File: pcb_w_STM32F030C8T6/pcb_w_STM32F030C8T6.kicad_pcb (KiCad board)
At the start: 2 copper layers, 32 parts, among them J1 Conn_01x04, J2 Conn_01x05, J3 USB_B_Micro, SW1 SW_Push, SW2 SW_SPDT, SW3 SW_Push, SW4 SW_Push, SW5 SW_Push, U1 STM32F030C8Tx, U2 IFX27001TFV33

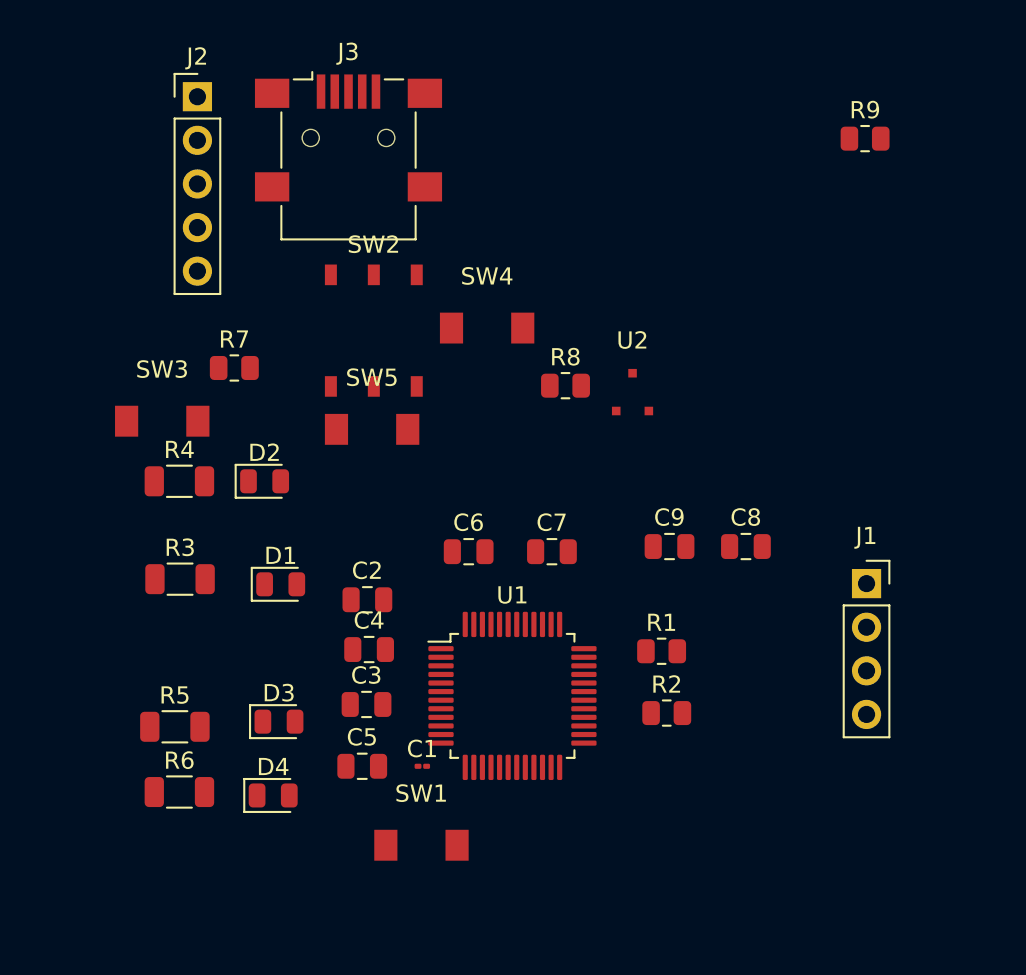
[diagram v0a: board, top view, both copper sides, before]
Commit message: made board 4 layers
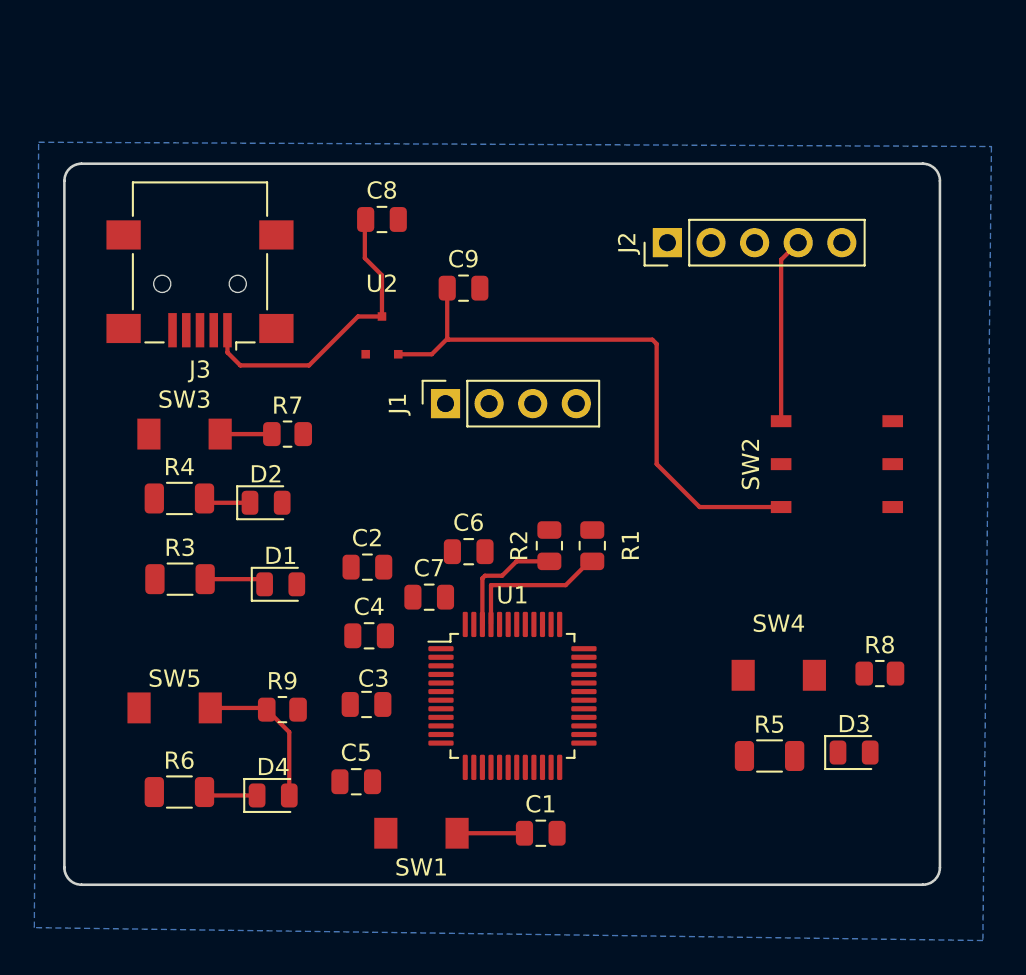
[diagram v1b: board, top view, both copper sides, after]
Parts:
- C1: footprint Capacitor_SMD:C_01005_0402Metric -> Capacitor_SMD:C_0805_2012Metric
- moved R9 47.5 mm to (55.7, 97.8)
- moved R5 34.7 mm to (84.1, 100.5)
- moved D3 33.5 mm to (89.0, 100.3)
- moved J2 28.7 mm to (78.1, 70.6), turned to 90 degrees
- moved C8 28.5 mm to (61.5, 69.2)
- moved SW2 28.1 mm to (88.0, 83.5), turned to 90 degrees
- moved J1 26.7 mm to (65.2, 80.0), turned to 90 degrees
- moved SW4 26.4 mm to (84.6, 95.8)
- moved R8 24.8 mm to (90.5, 95.7)
- moved SW5 19.9 mm to (49.4, 97.7)
- moved C9 19.2 mm to (66.2, 73.2)
- moved U2 15.0 mm to (61.5, 76.0)
- moved J3 12.1 mm to (50.9, 73.0), turned to 180 degrees
- moved R2 11.9 mm to (71.2, 88.2), turned to 90 degrees
- moved C1 7.93 mm to (70.8, 105.0)
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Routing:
- net MC_USB_3.3: track 0.00 -> 33.8 mm
- net MC_USB_5: track 0.00 -> 17.9 mm
- net Net-(J2-Pad4): track 0.00 -> 10.8 mm
- net DEC: track 0.00 -> 8.87 mm
- net SCL: track 0.00 -> 8.76 mm
- net SDA: track 0.00 -> 7.00 mm
- net NRST: track 0.00 -> 3.92 mm
- net Net-(D1-Pad1): track 0.00 -> 3.59 mm
- net Net-(D4-Pad1): track 0.00 -> 3.15 mm
- net CHANGE_STATE: track 0.00 -> 3.01 mm
- net Net-(D2-Pad1): track 0.00 -> 2.75 mm
- added copper zone on B.Cu, net GND
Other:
- board outline added: 51 x 42 mm

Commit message: saved
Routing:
- added copper zone on In1.Cu, net VDDA
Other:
- copper layers 2 -> 4
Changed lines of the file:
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@@
 (kicad_pcb (version 20211014) (generator pcbnew)
   (general
-    (thickness 1.6)
+    (thickness 4.69)
   )
   (paper "A4")
   (layers
     (0 "F.Cu" signal)
+    (1 "In1.Cu" signal)
+    (2 "In2.Cu" signal)
     (31 "B.Cu" signal)
     (32 "B.Adhes" user "B.Adhesive")
@@
       (layer "F.Cu" (type "copper") (thickness 0.035))
       (layer "dielectric 1" (type "core") (thickness 1.51) (material "FR4") (epsilon_r 4.5) (loss_tangent 0.02))
+      (layer "In1.Cu" (type "copper") (thickness 0.035))
+      (layer "dielectric 2" (type "prepreg") (thickness 1.51) (material "FR4") (epsilon_r 4.5) (loss_tangent 0.02))
+      (layer "In2.Cu" (type "copper") (thickness 0.035))
+      (layer "dielectric 3" (type "core") (thickness 1.51) (material "FR4") (epsilon_r 4.5) (loss_tangent 0.02))
       (layer "B.Cu" (type "copper") (thickness 0.035))
       (layer "B.Mask" (type "Bottom Solder Mask") (thickness 0.01))
@@
   (segment (start 77.25 76.25) (end 65.35 76.25) (width 0.25) (layer "F.Cu") (net 20))
   (segment (start 80 86) (end 77.5 83.5) (width 0.25) (layer "F.Cu") (net 20))
+  (zone (net 3) (net_name "VDDA") (layer "In1.Cu") (hatch edge 0.508)
+    (connect_pads (clearance 0.508))
+    (min_thickness 0.254) (filled_areas_thickness no)
+    (fill yes (thermal_gap 0.508) (thermal_bridge_width 0.508))
+    (polygon
+      (pts
+        (xy 97.043209 65.00317)
+        (xy 96.543209 111.25317)
+        (xy 41.293209 110.50317)
+        (xy 41.543209 64.75317)
+      )
+    )
+  )
   (zone (net 2) (net_name "GND") (layer "B.Cu") (hatch edge 0.508)
     (connect_pads (clearance 0.508))

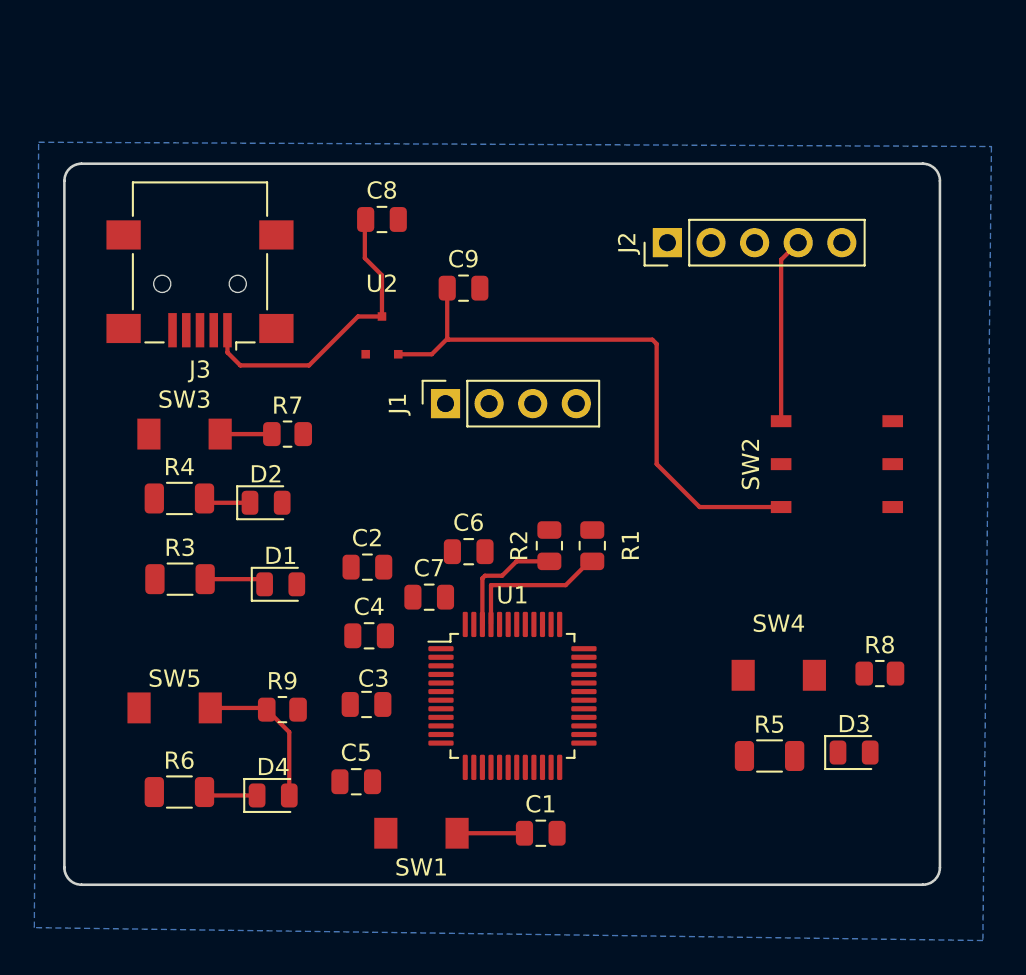
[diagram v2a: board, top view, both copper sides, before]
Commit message: finished routing...need to fix margins errors
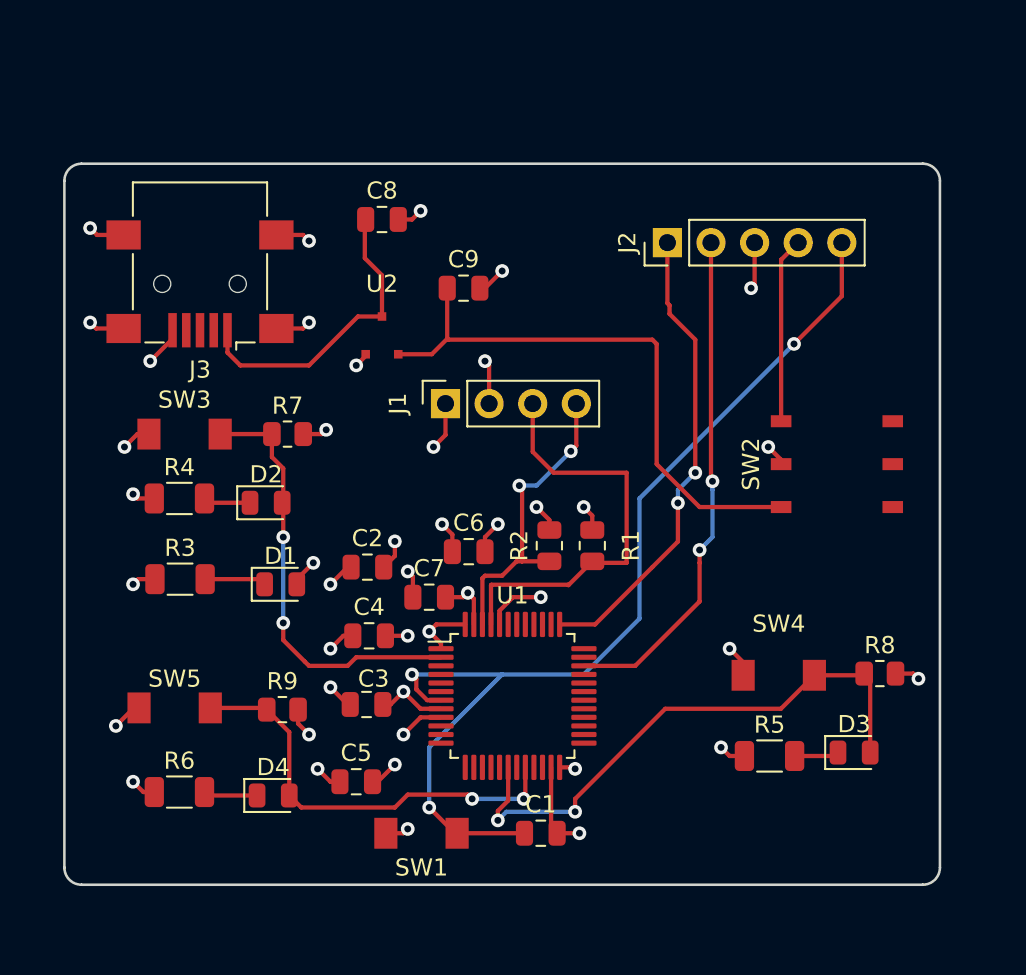
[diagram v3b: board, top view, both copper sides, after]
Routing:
- net NRST: track 3.92 -> 59.7 mm, vias 0 -> 3
- net GND: track 0.00 -> 55.1 mm, vias 0 -> 26
- net INC: track 0.00 -> 33.4 mm, vias 0 -> 2
- net VDDA: track 0.00 -> 31.1 mm, vias 0 -> 17
- net SWDIO: track 0.00 -> 29.5 mm, vias 0 -> 2
- net SWCLK: track 0.00 -> 27.4 mm, vias 0 -> 2
- net CHANGE_STATE: track 3.01 -> 25.4 mm, vias 0 -> 2
- net DEC: track 8.87 -> 25.1 mm, vias 0 -> 2
- net SCL: track 8.76 -> 24.8 mm
- net SDA: track 7.00 -> 18.2 mm, vias 0 -> 2
- net Net-(D3-Pad1): track 0.00 -> 2.61 mm
- added copper zone on In2.Cu, net GND
- removed copper zone on B.Cu, net GND

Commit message: finished routing and add silkscreen
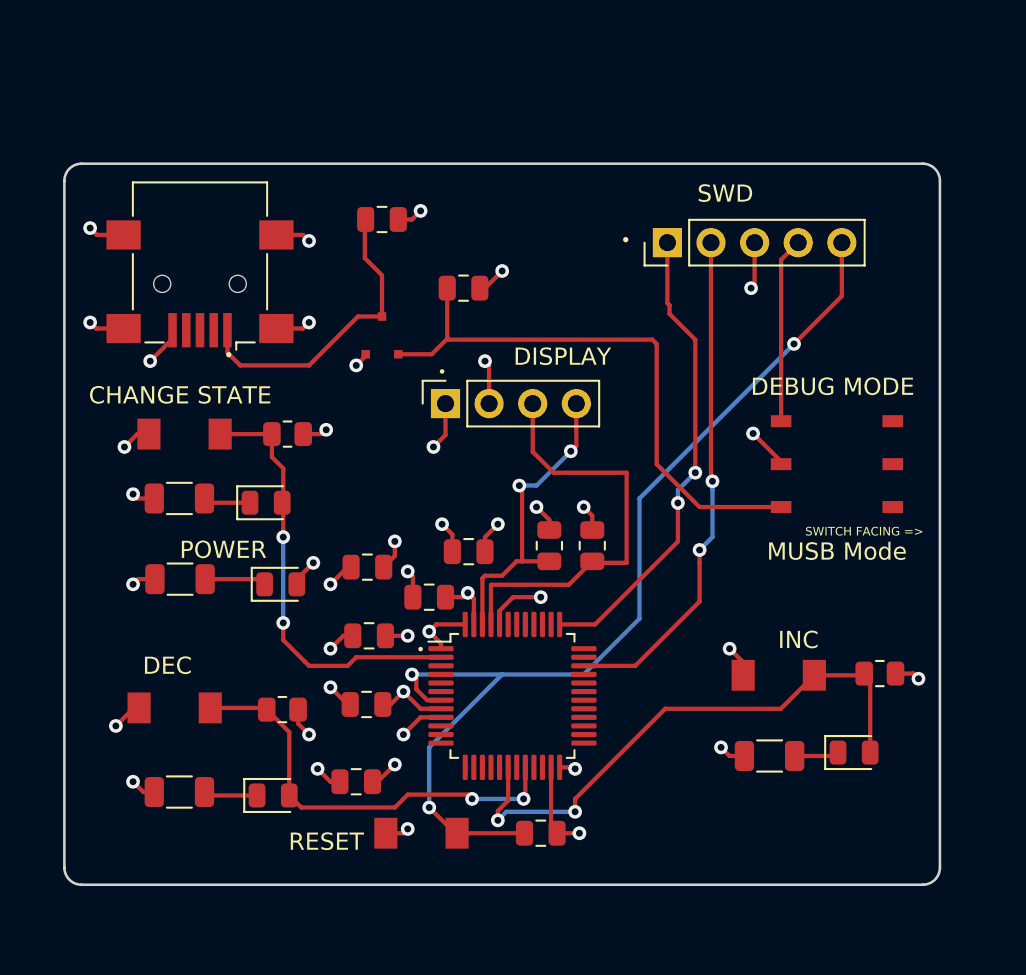
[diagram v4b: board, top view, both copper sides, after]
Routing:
- net VDDA: track 31.1 -> 32.2 mm
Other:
- board text added: "CHANGE STATE"
- board text added: "DEBUG MODE"
- board text added: "DEC"
- board text added: "DISPLAY"
- board text added: "INC"
- board text added: "MUSB Mode"
- board text added: "POWER"
- board text added: "RESET"
- board text added: "SWD"
- board text added: "SWITCH FACING =>"

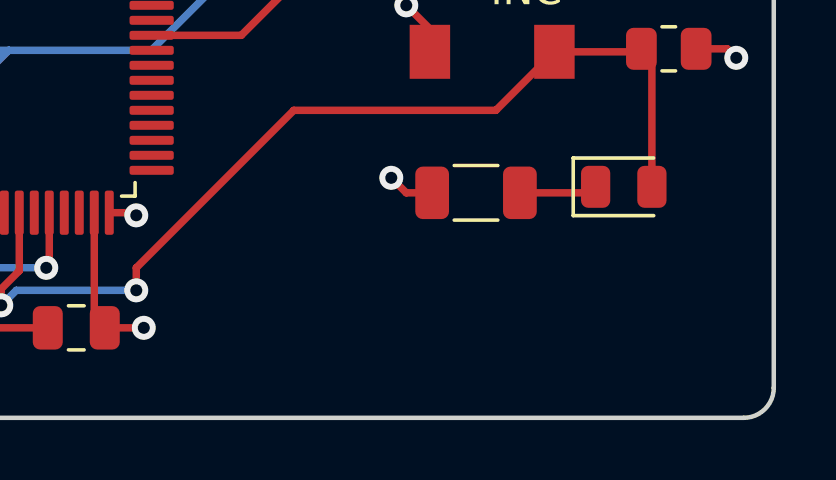
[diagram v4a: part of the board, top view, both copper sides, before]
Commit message: added batman logo
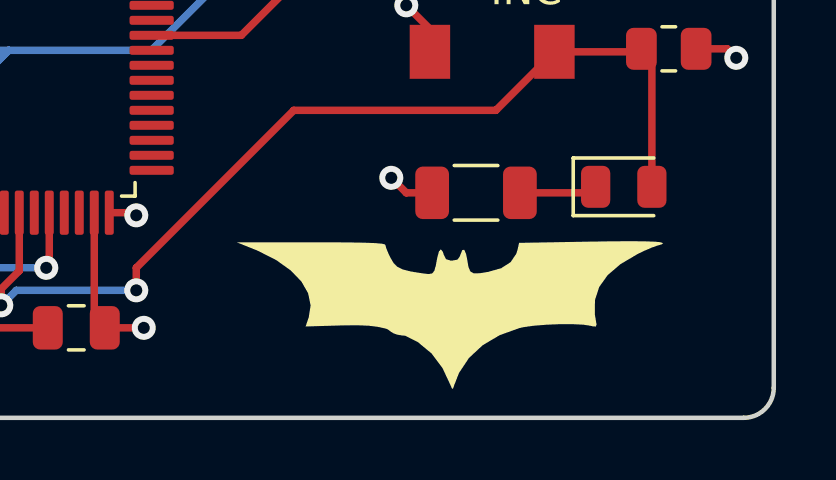
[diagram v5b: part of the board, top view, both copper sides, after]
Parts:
- added G***: LOGO, MyLibrary:batman, F.Cu at (83.2, 104.5)
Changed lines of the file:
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@@
     )
+  )
+  (footprint "MyLibrary:batman" (layer "F.Cu")
+    (at 83.2 104.525)
+    (attr board_only exclude_from_pos_files exclude_from_bom)
+    (fp_text reference "G***" (at 0 0) (layer "F.SilkS")
+      (effects (font (size 1.524 1.524) (thickness 0.3)))
+    )
+    (fp_text value "LOGO" (at 0.75 0) (layer "F.SilkS") hide
+      (effects (font (size 1.524 1.524) (thickness 0.3)))
+    )
+    (fp_poly (pts
+        (xy 6.508456 -2.408262)
+        (xy 6.840631 -2.395926)
+        (xy 7.040473 -2.37523)
+        (xy 7.113224 -2.345872)
+        (xy 7.064127 -2.307551)
+        (xy 6.931147 -2.267863)
+        (xy 6.747573 -2.204576)
+        (xy 6.490445 -2.094667)
+        (xy 6.264971 -1.986507)
+        (xy 5.689682 -1.646237)
+        (xy 5.262885 -1.280717)
+        (xy 4.98084 -0.88419)
+        (xy 4.839809 -0.4509)
+        (xy 4.836053 0.024908)
+        (xy 4.860795 0.175109)
+        (xy 4.892814 0.361587)
+        (xy 4.870314 0.433256)
+        (xy 4.769466 0.42568)
+        (xy 4.704088 0.409014)
+        (xy 4.451144 0.371153)
+        (xy 4.090608 0.353226)
+        (xy 3.666875 0.353846)
+        (xy 3.224339 0.371624)
+        (xy 2.807395 0.405171)
+        (xy 2.460437 0.453101)
+        (xy 2.32141 0.483513)
+        (xy 1.657705 0.723057)
+        (xy 1.093341 1.058742)
+        (xy 0.639672 1.48065)
+        (xy 0.308056 1.978861)
+        (xy 0.151358 2.378852)
+        (xy 0.106937 2.507714)
+        (xy 0.071644 2.497583)
+        (xy 0.038579 2.417221)
+        (xy -0.243247 1.815584)
+        (xy -0.604272 1.332313)
+        (xy -1.060125 0.953719)
+        (xy -1.626433 0.666111)
+        (xy -2.154119 0.496332)
+        (xy -2.415442 0.439846)
+        (xy -2.701705 0.40537)
+        (xy -3.050276 0.390593)
+        (xy -3.498523 0.393199)
+        (xy -3.726798 0.398959)
+        (xy -4.806165 0.430456)
+        (xy -4.701621 0.127014)
+        (xy -4.638694 -0.276442)
+        (xy -4.722196 -0.677422)
+        (xy -4.945201 -1.067404)
+        (xy -5.300783 -1.437868)
+        (xy -5.782016 -1.780293)
+        (xy -6.381972 -2.086159)
+        (xy -6.561027 -2.160422)
+        (xy -7.098187 -2.373569)
+        (xy -4.623414 -2.37621)
+        (xy -3.885422 -2.375334)
+        (xy -3.291482 -2.370754)
+        (xy -2.832206 -2.362149)
+        (xy -2.49821 -2.349197)
+        (xy -2.280106 -2.331576)
+        (xy -2.16851 -2.308965)
+        (xy -2.14864 -2.291335)
+        (xy -2.116411 -2.175343)
+        (xy -2.034587 -1.980043)
+        (xy -1.981157 -1.868466)
+        (xy -1.875592 -1.687719)
+        (xy -1.749816 -1.560955)
+        (xy -1.570839 -1.47192)
+        (xy -1.305669 -1.404355)
+        (xy -0.921317 -1.342007)
+        (xy -0.909237 -1.34028)
+        (xy -0.711627 -1.316815)
+        (xy -0.589448 -1.33513)
+        (xy -0.515752 -1.423761)
+        (xy -0.463589 -1.611245)
+        (xy -0.417605 -1.860876)
+        (xy -0.360894 -2.072742)
+        (xy -0.29608 -2.139601)
+        (xy -0.230515 -2.05823)
+        (xy -0.1987 -1.956797)
+        (xy -0.125696 -1.813659)
+        (xy 0.02692 -1.766246)
+        (xy 0.076737 -1.764954)
+        (xy 0.254176 -1.79625)
+        (xy 0.340159 -1.915022)
+        (xy 0.352174 -1.956797)
+        (xy 0.415116 -2.116178)
+        (xy 0.480811 -2.127207)
+        (xy 0.54162 -1.994655)
+        (xy 0.577636 -1.816018)
+        (xy 0.62369 -1.553424)
+        (xy 0.6874 -1.401655)
+        (xy 0.80335 -1.33939)
+        (xy 1.006124 -1.345306)
+        (xy 1.272027 -1.387921)
+        (xy 1.715398 -1.513101)
+        (xy 2.028628 -1.713849)
+        (xy 2.217581 -1.994618)
+        (xy 2.261814 -2.139842)
+        (xy 2.309532 -2.357102)
+        (xy 4.665491 -2.398123)
+        (xy 5.426129 -2.409059)
+        (xy 6.038703 -2.412539)
+      ) (layer "F.SilkS") (width 0) (fill solid))
   )
   (footprint "Capacitor_SMD:C_0805_2012Metric" (layer "F.Cu")
